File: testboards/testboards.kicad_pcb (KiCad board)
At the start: 2 copper layers, 39.4 x 43.2 mm, 0 parts

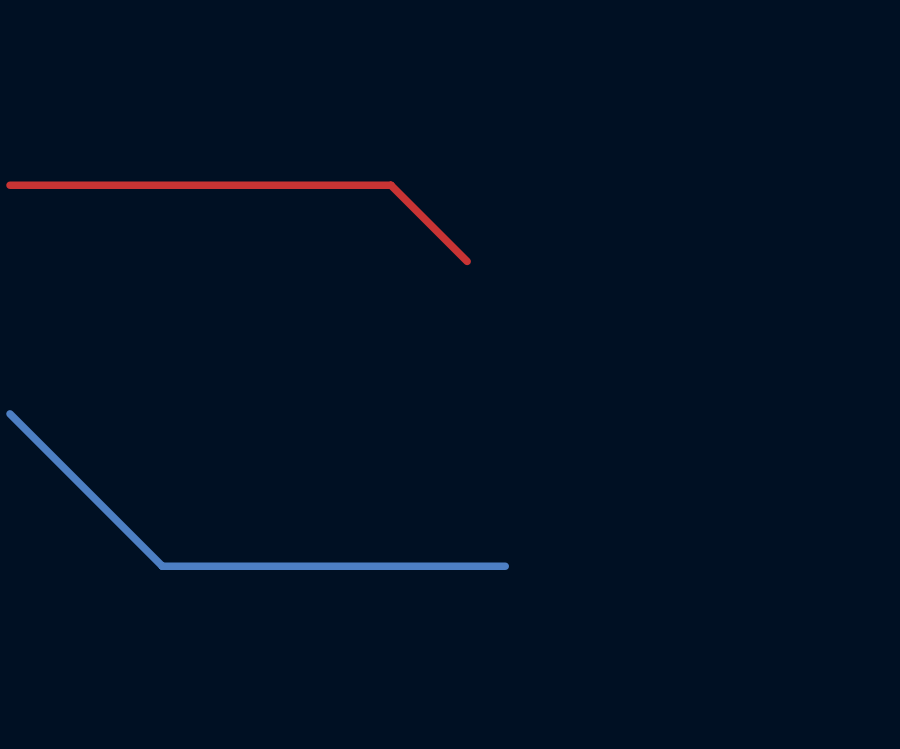
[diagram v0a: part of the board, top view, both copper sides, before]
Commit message: Added finding smallest trace
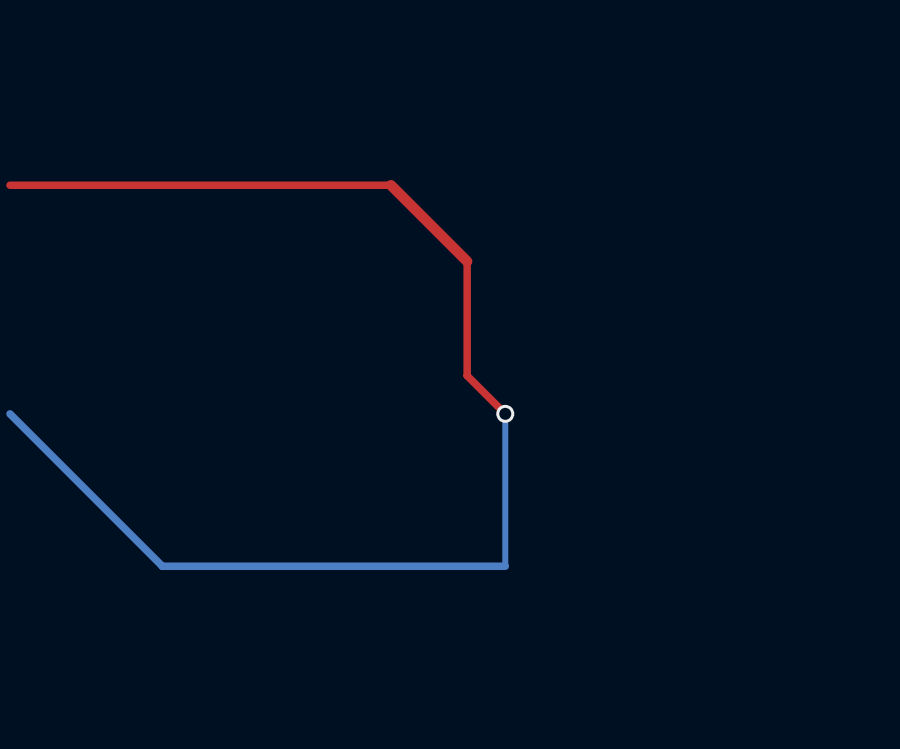
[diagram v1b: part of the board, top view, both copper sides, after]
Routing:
- net (no net): track 34.9 -> 45.6 mm, vias 0 -> 1
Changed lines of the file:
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@@
     (thickness 1.6)
     (drawings 8)
-    (tracks 4)
+    (tracks 8)
     (zones 0)
     (modules 0)
@@
   (gr_line (start 57.15 21.59) (end 57.15 64.77) (angle 90) (layer Edge.Cuts) (width 0.15))
   (gr_line (start 19.05 21.59) (end 57.15 21.59) (angle 90) (layer Edge.Cuts) (width 0.15))
+  (segment (start 40.64 30.48) (end 40.64 34.29) (width 0.25) (layer F.Cu) (net 0))
+  (segment (start 38.1 27.94) (end 40.64 30.48) (width 0.35) (layer F.Cu) (net 0))
+  (segment (start 25.4 27.94) (end 38.1 27.94) (width 0.25) (layer F.Cu) (net 0))
+  (segment (start 30.48 40.64) (end 25.4 35.56) (width 0.25) (layer B.Cu) (net 0))
   (segment (start 41.91 40.64) (end 30.48 40.64) (width 0.25) (layer B.Cu) (net 0))
-  (segment (start 30.48 40.64) (end 25.4 35.56) (width 0.25) (layer B.Cu) (net 0))
-  (segment (start 25.4 27.94) (end 38.1 27.94) (width 0.25) (layer F.Cu) (net 0))
-  (segment (start 38.1 27.94) (end 40.64 30.48) (width 0.25) (layer F.Cu) (net 0))
+  (segment (start 41.91 35.56) (end 41.91 40.64) (width 0.20) (layer B.Cu) (net 0))
+  (via (at 41.91 35.56) (size 0.6) (drill 0.4) (layers F.Cu B.Cu) (net 0))
+  (segment (start 40.64 34.29) (end 41.91 35.56) (width 0.25) (layer F.Cu) (net 0))
 )
